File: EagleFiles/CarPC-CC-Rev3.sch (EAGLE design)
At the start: 72 parts, among them IC10 RN42HID-I/RM, IC2 MCP2515-I_SO, IC3 TJA1050T-CM/118, IC4 INA219AIDR, K1 G3VM-61VR(TR), Q5 16MHz

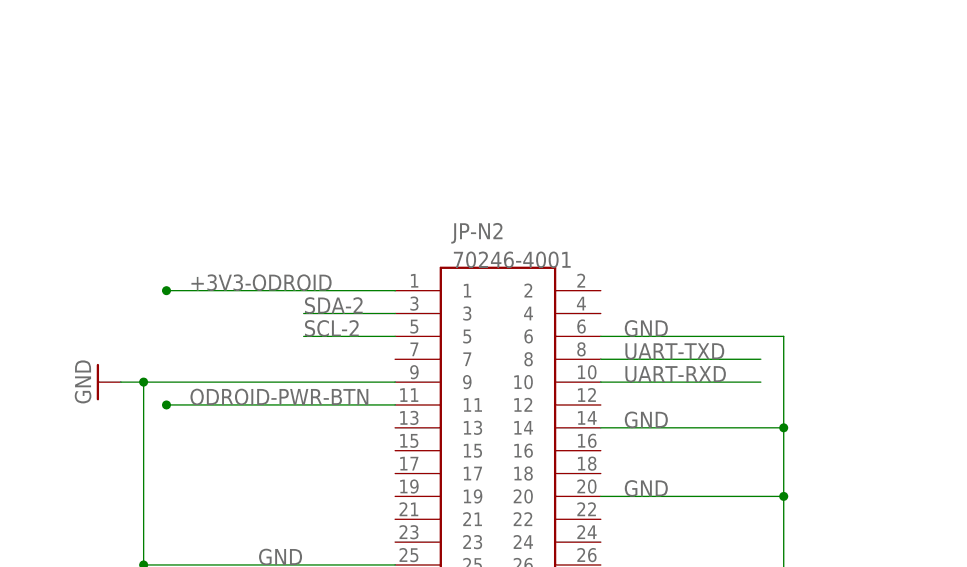
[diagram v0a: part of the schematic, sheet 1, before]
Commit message: Error in schemic and board: using 5v rail now
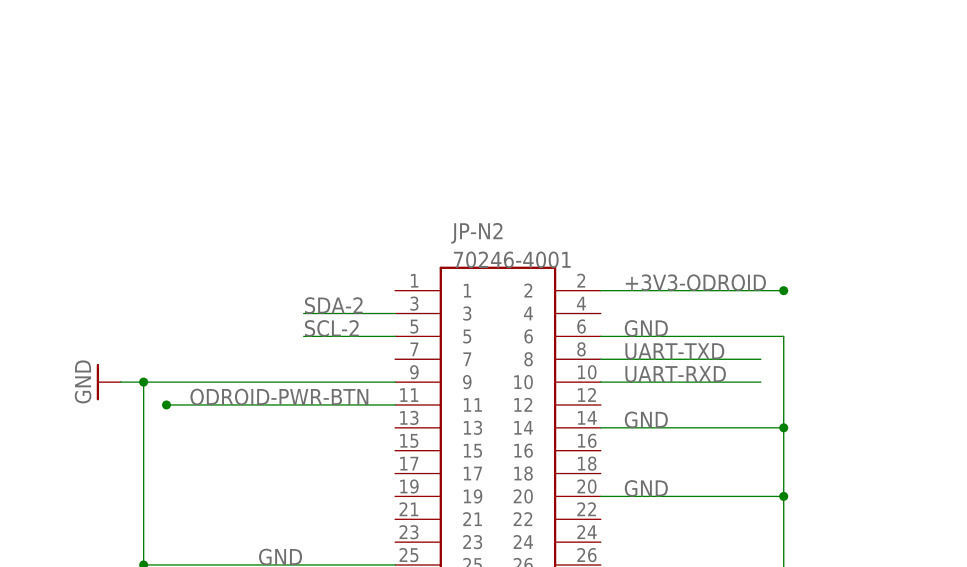
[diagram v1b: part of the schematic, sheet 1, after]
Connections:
- net +3V3-ODROID: now also JP-N2.2; no longer JP-N2.1
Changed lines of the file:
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@@
 </segment>
 <segment>
-<pinref part="JP-N2" gate="G$1" pin="1"/>
-<wire x1="-137.16" y1="233.68" x2="-111.76" y2="233.68" width="0.1524" layer="91" grouprefs="ODROID-N2-HEADER"/>
-<label x="-134.62" y="233.68" size="1.778" layer="95" grouprefs="ODROID-N2-HEADER"/>
-<junction x="-137.16" y="233.68" grouprefs="ODROID-N2-HEADER"/>
+<pinref part="JP-N2" gate="G$1" pin="2"/>
+<wire x1="-88.9" y1="233.68" x2="-68.58" y2="233.68" width="0.1524" layer="91"/>
+<label x="-86.36" y="233.68" size="1.778" layer="95"/>
+<junction x="-68.58" y="233.68"/>
 </segment>
 </net>

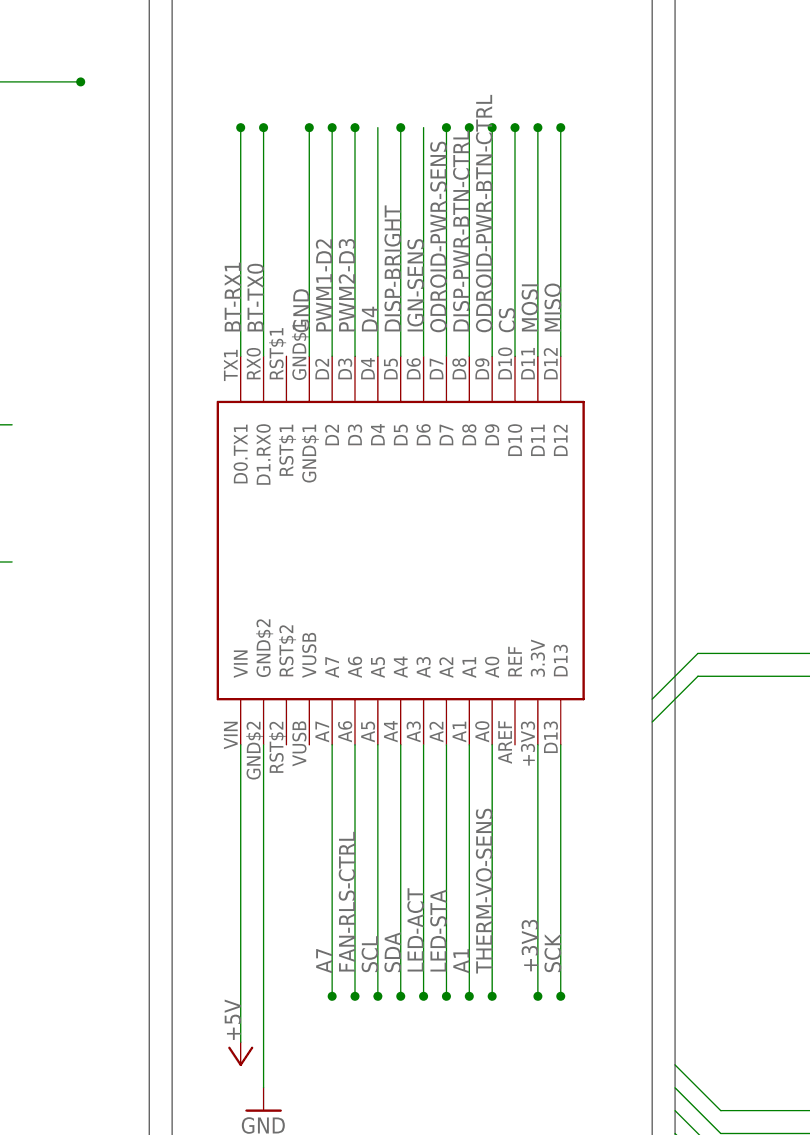
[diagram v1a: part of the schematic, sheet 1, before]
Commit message: Fan control interferes with display brightness.
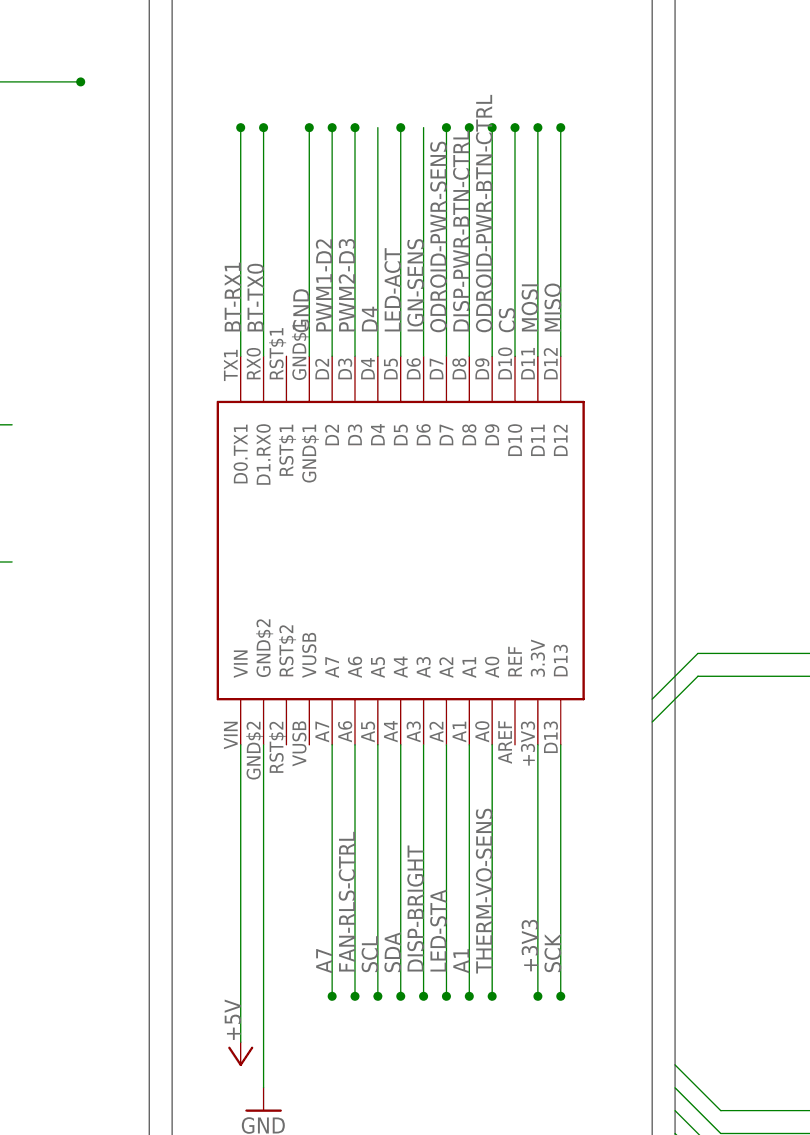
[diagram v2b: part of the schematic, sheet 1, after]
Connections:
- net DISP-BRIGHT: now also NANO_33_IOT.A3; no longer NANO_33_IOT.D5
- net LED-ACT: now also NANO_33_IOT.D5; no longer NANO_33_IOT.A3
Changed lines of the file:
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@@
 </segment>
 <segment>
-<pinref part="NANO_33_IOT" gate="G$1" pin="D5"/>
-<label x="0" y="93.98" size="1.778" layer="95" rot="R90" grouprefs="ARDUINO_NANO_33_IOT"/>
-<wire x1="0" y1="91.44" x2="0" y2="116.84" width="0.1524" layer="91" grouprefs="ARDUINO_NANO_33_IOT"/>
-<junction x="0" y="116.84" grouprefs="ARDUINO_NANO_33_IOT"/>
+<wire x1="2.54" y1="48.26" x2="2.54" y2="20.32" width="0.1524" layer="91" grouprefs="ARDUINO_NANO_33_IOT"/>
+<pinref part="NANO_33_IOT" gate="G$1" pin="A3"/>
+<label x="2.54" y="22.86" size="1.778" layer="95" rot="R90" grouprefs="ARDUINO_NANO_33_IOT"/>
+<junction x="2.54" y="20.32" grouprefs="ARDUINO_NANO_33_IOT"/>
 </segment>
 </net>
@@
 <net name="LED-ACT" class="0">
 <segment>
-<wire x1="2.54" y1="48.26" x2="2.54" y2="20.32" width="0.1524" layer="91" grouprefs="ARDUINO_NANO_33_IOT"/>
-<pinref part="NANO_33_IOT" gate="G$1" pin="A3"/>
-<label x="2.54" y="22.86" size="1.778" layer="95" rot="R90" grouprefs="ARDUINO_NANO_33_IOT"/>
-<junction x="2.54" y="20.32" grouprefs="ARDUINO_NANO_33_IOT"/>
-</segment>
-<segment>
 <wire x1="220.98" y1="-17.78" x2="254" y2="-17.78" width="0.1524" layer="91" grouprefs="LED1"/>
 <label x="254" y="-15.24" size="1.778" layer="95" rot="R180" grouprefs="LED1"/>
 <pinref part="ACT" gate="G$1" pin="A"/>
 </segment>
+<segment>
+<pinref part="NANO_33_IOT" gate="G$1" pin="D5"/>
+<label x="0" y="93.98" size="1.778" layer="95" rot="R90" grouprefs="ARDUINO_NANO_33_IOT"/>
+<wire x1="0" y1="91.44" x2="0" y2="116.84" width="0.1524" layer="91" grouprefs="ARDUINO_NANO_33_IOT"/>
+<junction x="0" y="116.84" grouprefs="ARDUINO_NANO_33_IOT"/>
+</segment>
 </net>
